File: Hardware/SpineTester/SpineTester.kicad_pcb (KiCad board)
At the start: 2 copper layers, 5 parts, among them P1 USB_C_Plug_USB2.0, U1 RP2040, U2 HX711, U3 HX711, U4 CH340C

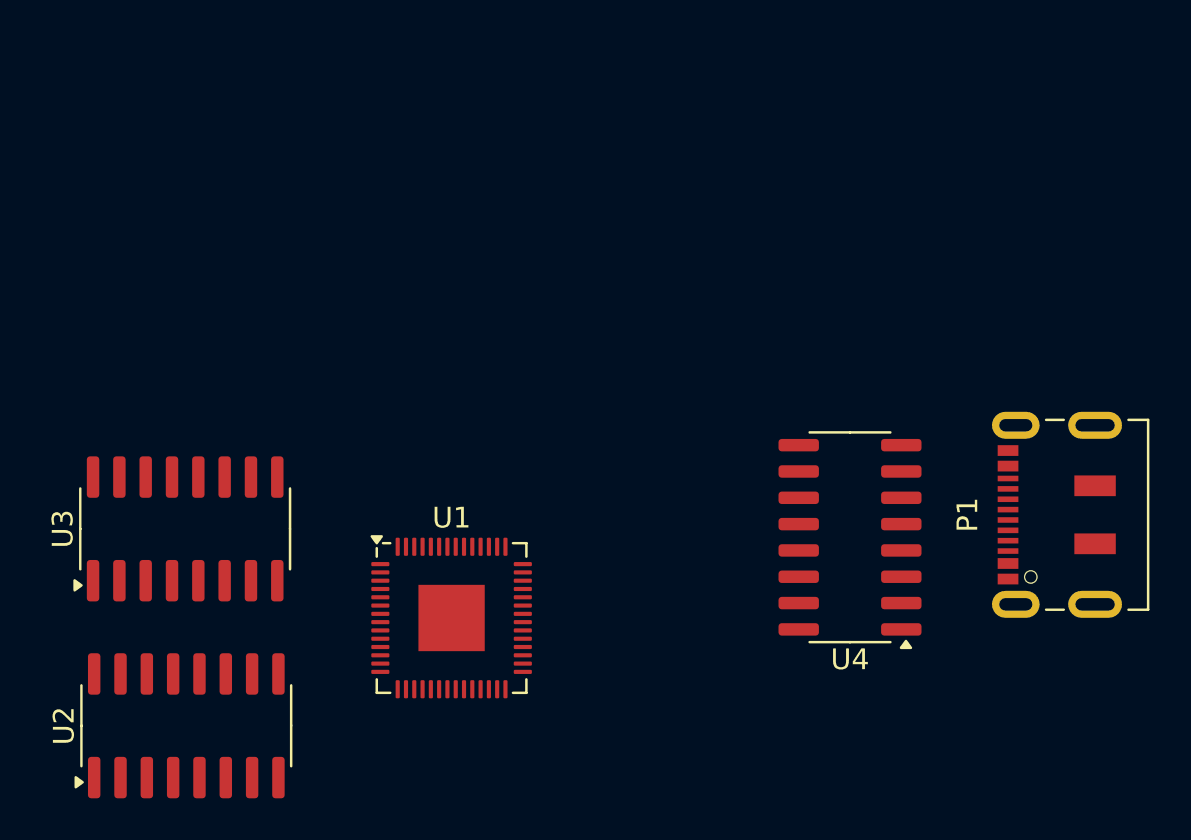
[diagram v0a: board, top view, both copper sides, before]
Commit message: added connectors
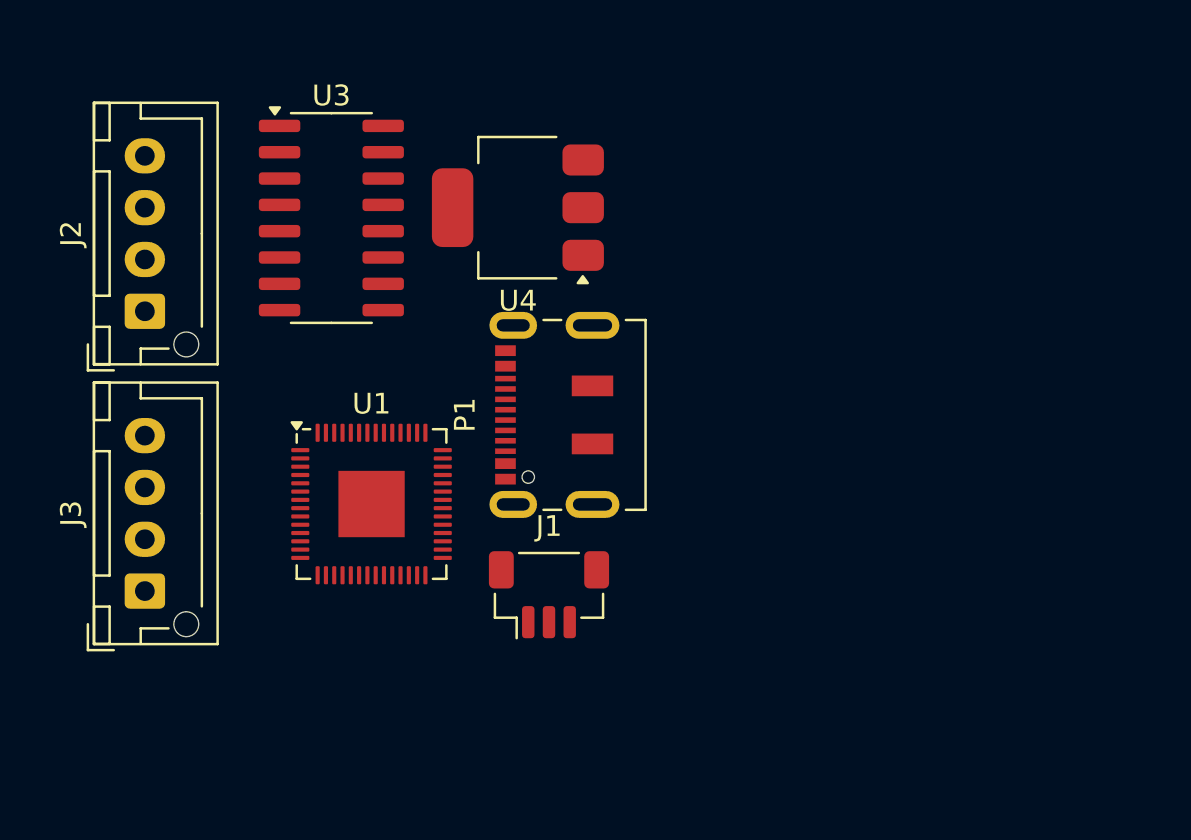
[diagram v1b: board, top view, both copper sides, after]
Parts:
- removed U2: HX711, Package_SO:SOP-16_3.9x9.9mm_P1.27mm
- added J1: Conn_01x03_Socket, Connector_JST:JST_SH_BM03B-SRSS-TB_1x03-1MP_P1.00mm_Vertical, F.Cu at (111.5, 57.2)
- added J2: Conn_01x04, Connector_JST:JST_XH_B4B-XH-AM_1x04_P2.50mm_Vertical, F.Cu at (92.0, 43.5)
- added J3: Conn_01x04, Connector_JST:JST_XH_B4B-XH-AM_1x04_P2.50mm_Vertical, F.Cu at (92.0, 57.0)
- U4: value CH340C -> AMS1117; footprint Package_SO:SOIC-16_3.9x9.9mm_P1.27mm -> Package_TO_SOT_SMD:SOT-223-3_TabPin2
- moved P1 24.7 mm to (112.5, 48.5)
- moved U4 22.6 mm to (110.0, 38.5)
- moved U3 16.6 mm to (101.0, 39.0), turned to 0 degrees
- moved U1 6.72 mm to (102.9, 52.8)
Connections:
- P1 pad A1: Net-(P1-GND-PadA1) -> GND
- P1 pad A12: Net-(P1-GND-PadA1) -> GND
- P1 pad A4: Net-(P1-VBUS-PadA4) -> Net-(U4-VI)
- P1 pad A9: Net-(P1-VBUS-PadA4) -> Net-(U4-VI)
- P1 pad B1: Net-(P1-GND-PadA1) -> GND
- P1 pad B12: Net-(P1-GND-PadA1) -> GND
- P1 pad B4: Net-(P1-VBUS-PadA4) -> Net-(U4-VI)
- P1 pad B9: Net-(P1-VBUS-PadA4) -> Net-(U4-VI)
- P1 pad S1: unconnected-(P1-SHIELD-PadS1) -> GND
- U1 pad 1: Net-(U1-IOVDD-Pad1) -> +3.3V
- U1 pad 10: Net-(U1-IOVDD-Pad1) -> +3.3V
- U1 pad 22: Net-(U1-IOVDD-Pad1) -> +3.3V
- U1 pad 24: unconnected-(U1-SWCLK-Pad24) -> Net-(J1-Pin_3)
- U1 pad 25: unconnected-(U1-SWD-Pad25) -> Net-(J1-Pin_1)
- U1 pad 33: Net-(U1-IOVDD-Pad1) -> +3.3V
- U1 pad 42: Net-(U1-IOVDD-Pad1) -> +3.3V
- U1 pad 43: unconnected-(U1-ADC_AVDD-Pad43) -> +3.3V
- U1 pad 44: unconnected-(U1-VREG_IN-Pad44) -> +3.3V
- U1 pad 46: unconnected-(U1-USB_DM-Pad46) -> Net-(P1-D-)
- U1 pad 47: unconnected-(U1-USB_DP-Pad47) -> Net-(P1-D+)
- U1 pad 48: unconnected-(U1-USB_VDD-Pad48) -> +3.3V
- U1 pad 49: Net-(U1-IOVDD-Pad1) -> +3.3V
- U1 pad 57: unconnected-(U1-GND-Pad57) -> GND
- U3 pad 1: unconnected-(U3-VSUP-Pad1) -> +3.3V
- U3 pad 10: unconnected-(U3-INB+-Pad10) -> Net-(J3-Pin_3)
- U3 pad 16: unconnected-(U3-DVDD-Pad16) -> +3.3V
- U3 pad 5: unconnected-(U3-AGND-Pad5) -> GND
- U3 pad 7: unconnected-(U3-INA--Pad7) -> Net-(J2-Pin_2)
- U3 pad 8: unconnected-(U3-INA+-Pad8) -> Net-(J2-Pin_3)
- U3 pad 9: unconnected-(U3-INB--Pad9) -> Net-(J3-Pin_2)
- U4 pad 1: unconnected-(U4-GND-Pad1) -> GND
- U4 pad 2: unconnected-(U4-TXD-Pad2) -> +3.3V
- U4 pad 3: unconnected-(U4-RXD-Pad3) -> Net-(U4-VI)

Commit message: changed connectors
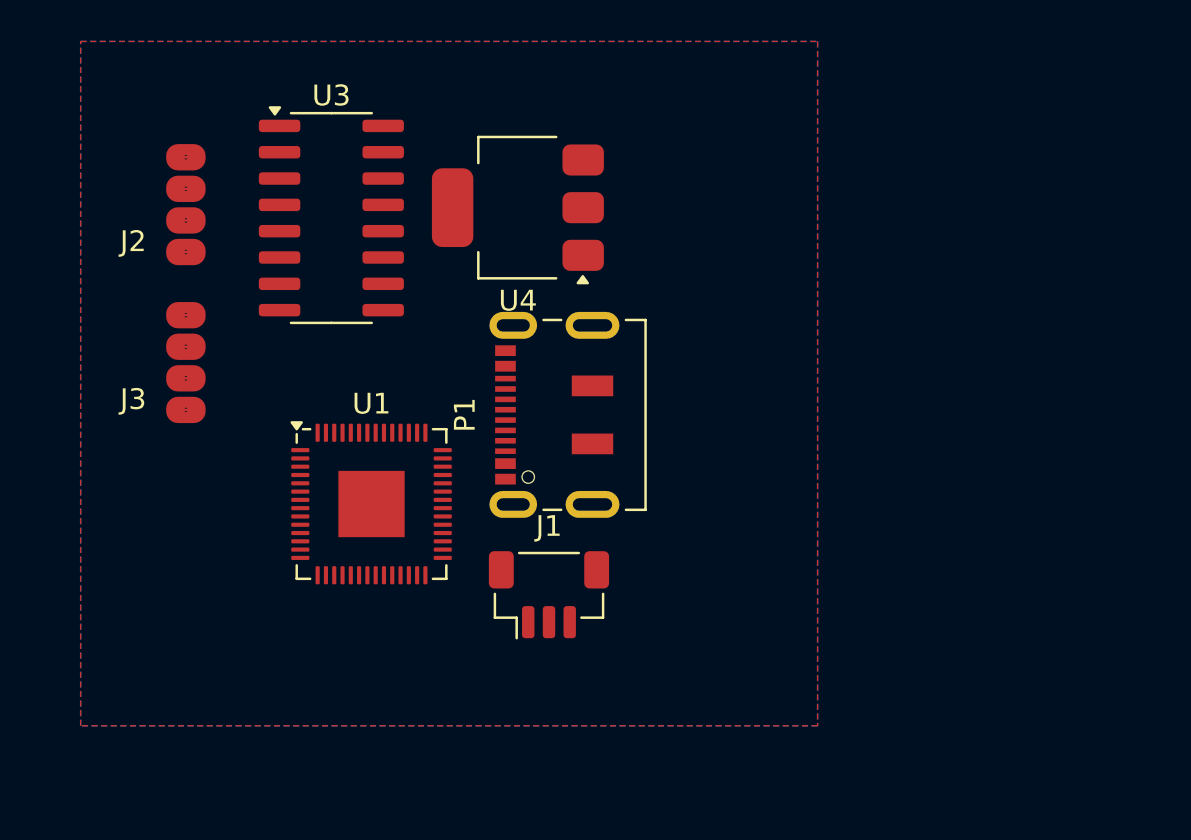
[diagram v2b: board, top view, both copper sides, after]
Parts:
- J2, J3: footprint Connector_JST:JST_XH_B4B-XH-AM_1x04_P2.50mm_Vertical -> Library:Solderpad
- moved J3 8.96 mm to (94.0, 48.3), turned to 0 degrees
- moved J2 3.48 mm to (94.0, 40.6), turned to 0 degrees
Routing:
- added copper zone on B.Cu, net GND
- added copper zone on F.Cu, net GND
